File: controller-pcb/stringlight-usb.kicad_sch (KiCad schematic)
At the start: 45 parts, among them J1 USB_B, J2 Conn_01x05, J3 Screw_Terminal_01x03, J4 Screw_Terminal_01x03, Q2 BC817, Q3 MJD31, Q4 MJD31, Q5 BC817, U1 PSSI2021SAY, U2 MCP1703Ax-330xxTT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

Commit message: enclosure
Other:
- note added: "enclosure: Euroclamp CEM17-S1-GY"
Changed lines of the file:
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@@
 	(generator_version "9.0")
 	(paper "A4")
+	(text "enclosure: Euroclamp CEM17-S1-GY"
+		(exclude_from_sim no)
+		(at 43.688 156.21 0)
+		(effects
+			(font
+				(size 1.27 1.27)
+			)
+		)
+	)
 	(junction
 		(at 217.17 87.63)

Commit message: connector
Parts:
- J3, J4: value Screw_Terminal_01x03 -> ML253-5-D-LC-BK
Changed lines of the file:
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@@
 			)
 		)
-		(property "Value" "Screw_Terminal_01x03"
+		(property "Value" "ML253-5-D-LC-BK"
 			(at 24.892 68.072 90)
 			(effects
@@
 			)
 		)
-		(property "Value" "Screw_Terminal_01x03"
+		(property "Value" "ML253-5-D-LC-BK"
 			(at 24.892 129.032 90)
 			(effects

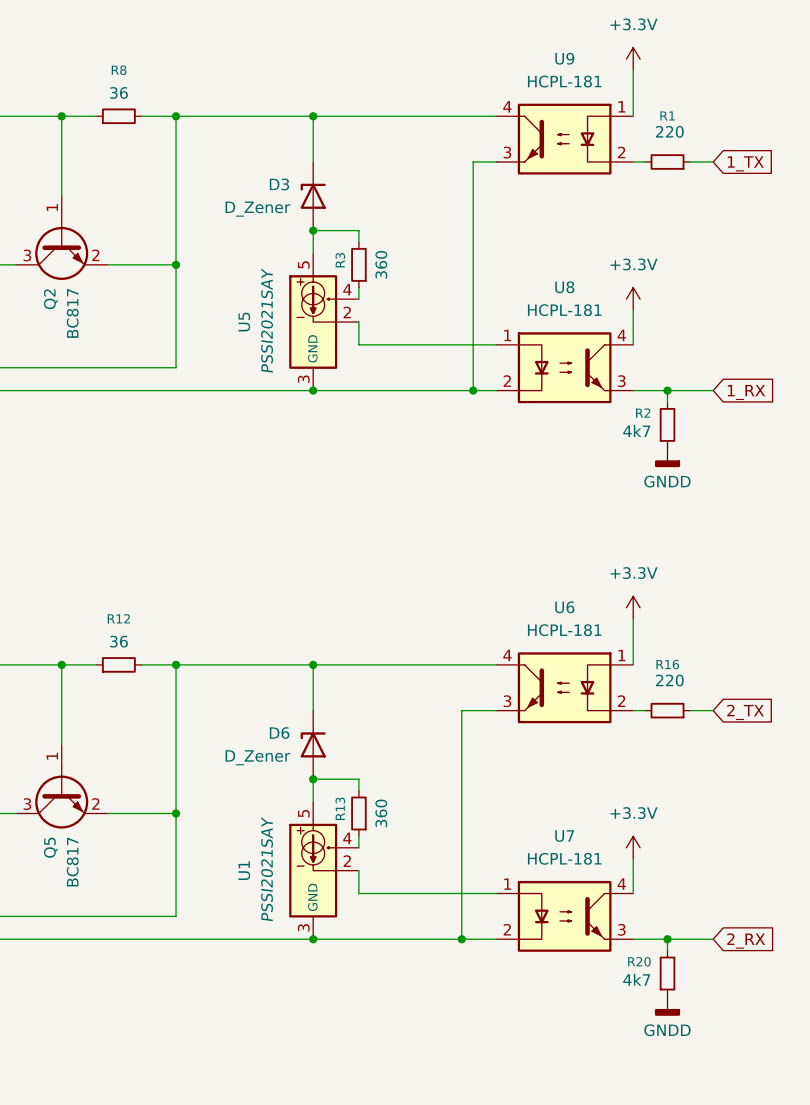
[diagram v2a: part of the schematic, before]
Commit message: - speed up opto RX with additional 1k resistor - add firmware-based 24V-data short circuit protection (goes into fault mode)
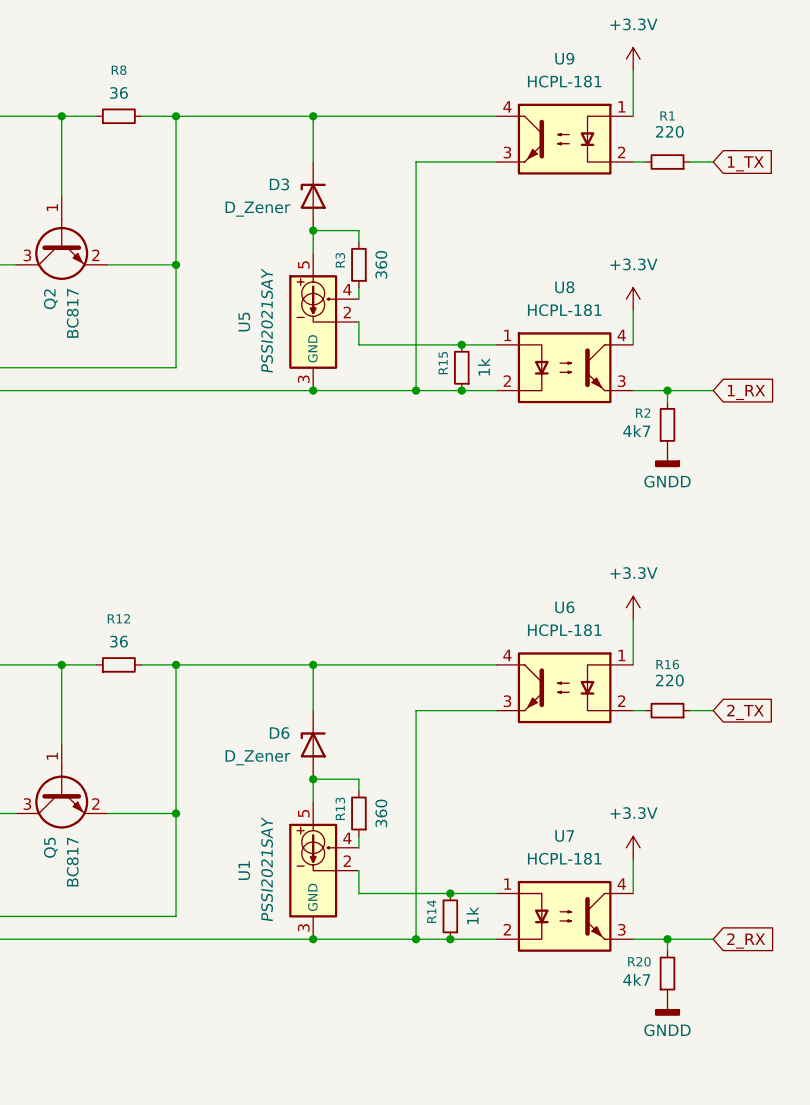
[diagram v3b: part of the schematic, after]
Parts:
- added R14, R15: 1k, Resistor_SMD:R_0603_1608Metric_Pad0.98x0.95mm_HandSolder, symbol Device:R_Small
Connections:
- net 1_GND: now also R15.1
- net 2_GND: now also R14.1
- net at U5.2, U8.1: now also R15.2
- net at U1.2, U7.1: now also R14.2
